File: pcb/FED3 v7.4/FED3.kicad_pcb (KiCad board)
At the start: 4 copper layers, 108 x 50 mm, 89 parts, among them IC1 MC74VHC1GT125, IC2 TB6612FNG, IC4 RTC PCF8523T, J1 Conn_02x03_Odd_Even, Q2 DMP2035U-7, SW1 Sw, SW2 SPST_TACT-KMR2, U1 ATSAMD21G18A, U2 MIC5504-3.3, U3 MCP73831T, X1 ClockXtal, X2 uXtal, X4 microsd, X5 JST-XH-02

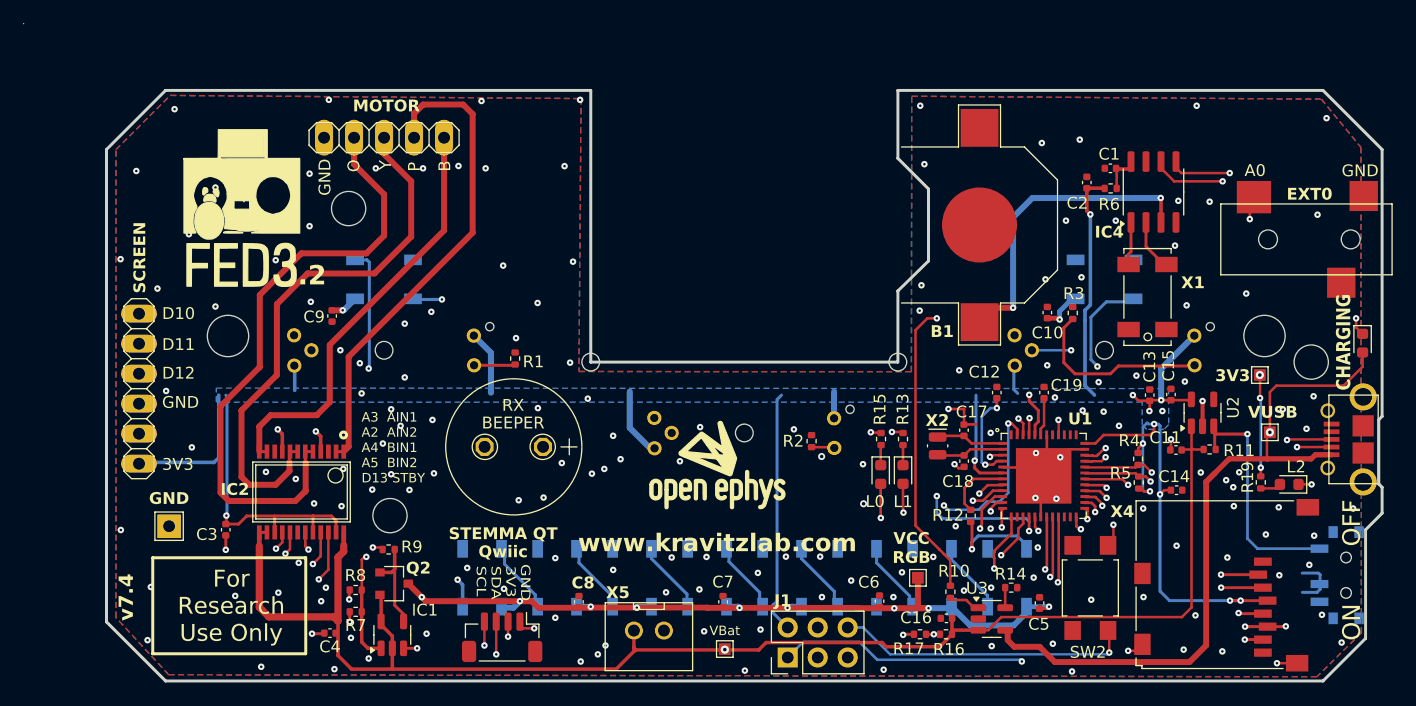
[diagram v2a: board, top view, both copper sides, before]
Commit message: last tunnings
- Top & Bottom Fabrication Layers tuned
- generated Gerbers&Drills files
- generated P&P & BOM files
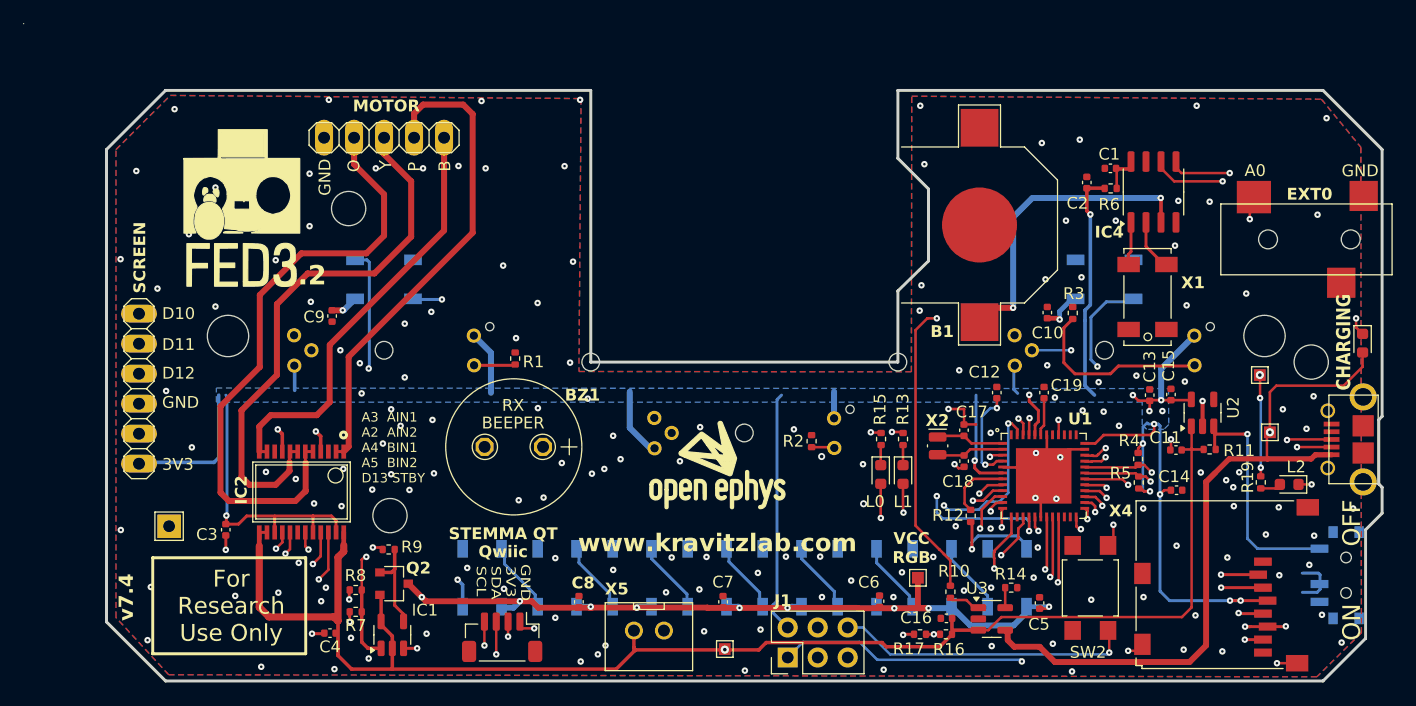
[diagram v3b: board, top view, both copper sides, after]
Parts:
- moved ? 20.0 mm to (192.5, 100.8)
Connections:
- net /controler stage/AREF renamed /Controller Stage/AREF
- net /controler stage/D10 renamed /Controller Stage/D10
- net /controler stage/D11 renamed /Controller Stage/D11
- net /controler stage/D12 renamed /Controller Stage/D12
- net /controler stage/D7 renamed /Controller Stage/D7
- net /controler stage/MISO renamed /Controller Stage/MISO
- net /controler stage/MOSI renamed /Controller Stage/MOSI
- net /controler stage/SCK renamed /Controller Stage/SCK
- net /controler stage/SCL renamed /Controller Stage/SCL
- net /controler stage/SDA renamed /Controller Stage/SDA
- net /controler stage/SD_CS renamed /Controller Stage/SD_CS
- net /controler stage/SQW renamed /Controller Stage/SQW
- net /controler stage/SWCLK renamed /Controller Stage/SWCLK
- net /controler stage/SWDIO renamed /Controller Stage/SWDIO
- net /controler stage/~{RESET} renamed /Controller Stage/~{RESET}

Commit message: 'ultima versão revista; não em tunning com a versão oficial /Kravitz/FED3
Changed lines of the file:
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@@
 		(sheetname "/Controller Stage/")
 		(sheetfile "controler stage.kicad_sch")
+		(attr smd)
 		(fp_circle
 			(center 0 0)
@@
 		(sheetname "/IOs Interface/")
 		(sheetfile "IOs Interface.kicad_sch")
+		(attr smd)
 		(fp_line
 			(start -1.45 0.8)
@@
 			)
 		)
-		(property "MPN" "TB6612FNG,C,8,EL "
+		(property "MPN" "TB6612FNG,C,8,EL"
 			(at 0 0 180)
 			(unlocked yes)
@@
 		(sheetname "/")
 		(sheetfile "FED3.kicad_sch")
+		(attr smd)
 		(fp_line
 			(start 4.128 2.536)
@@
 			)
 		)
-		(property "MPN" "ECS-.327-12.5-17X-C-TR "
+		(property "MPN" "ECS-.327-12.5-17X-C-TR"
 			(at 0 0 270)
 			(unlocked yes)
@@
 		(sheetname "/Controller Stage/")
 		(sheetfile "controler stage.kicad_sch")
+		(attr smd)
 		(fp_line
 			(start -4.1 2)
@@
 			)
 		)
-		(property "Description" "DC DC CONVERTER Boost/Inverter 2output ±40V 1.3A"
+		(property "Description" "BUFFER NON-INVERT 1CH 3-STATE"
 			(at 0 0 90)
 			(unlocked yes)
@@
 		(sheetname "/")
 		(sheetfile "FED3.kicad_sch")
-		(attr through_hole)
+		(attr smd)
 		(fp_line
 			(start -3.75 -2.9)
@@
 		(sheetname "/")
 		(sheetfile "FED3.kicad_sch")
-		(attr through_hole exclude_from_bom)
+		(attr through_hole)
 		(fp_line
 			(start -6.35 -0.635)
@@
 		(sheetname "/IOs Interface/")
 		(sheetfile "IOs Interface.kicad_sch")
-		(attr smd exclude_from_pos_files)
+		(attr smd)
 		(fp_line
 			(start 11 3)
@@
 			)
 		)
-		(property "MPN" "SK6812RGBW-BW"
+		(property "MPN" "XT1511RGBW-BW"
 			(at 0 0 180)
 			(unlocked yes)
@@
 			)
 		)
-		(property "MPN" "SK6812RGBW-BW"
+		(property "MPN" "XT1511RGBW-BW"
 			(at 0 0 270)
 			(unlocked yes)
@@
 			)
 		)
-		(property "MPN" "SSSS811101 "
+		(property "MPN" "SSSS811101"
 			(at 0 0 270)
 			(unlocked yes)
@@
 		(sheetname "/")
 		(sheetfile "FED3.kicad_sch")
+		(attr smd)
 		(fp_line
 			(start -3.4 1.75)
@@
 			)
 		)
-		(property "MPN" "SK6812RGBW-BW"
+		(property "MPN" "XT1511RGBW-BW"
 			(at 0 0 180)
 			(unlocked yes)
@@
 			)
 		)
-		(property "MPN" "SK6812RGBW-BW"
+		(property "MPN" "XT1511RGBW-BW"
 			(at 0 0 270)
 			(unlocked yes)
@@
 			)
 		)
-		(property "MPN" "SK6812RGBW-BW"
+		(property "MPN" "XT1511RGBW-BW"
 			(at 0 0 270)
 			(unlocked yes)
@@
 			)
 		)
-		(property "MPN" "SK6812RGBW-BW"
+		(property "MPN" "XT1511RGBW-BW"
 			(at 0 0 270)
 			(unlocked yes)
@@
 			)
 		)
-		(property "MPN" "SK6812RGBW-BW"
+		(property "MPN" "XT1511RGBW-BW"
 			(at 0 0 270)
 			(unlocked yes)
@@
 			)
 		)
-		(property "MPN" "SK6812RGBW-BW"
+		(property "MPN" "XT1511RGBW-BW"
 			(at 0 0 270)
 			(unlocked yes)
@@
 			)
 		)
-		(property "MPN" "SK6812RGBW-BW"
+		(property "MPN" "XT1511RGBW-BW"
 			(at 0 0 270)
 			(unlocked yes)
@@
 			)
 		)
-		(property "MPN" "SK6812RGBW-BW"
+		(property "MPN" "XT1511RGBW-BW"
 			(at 0 0 270)
 			(unlocked yes)
@@
 		)
 		(layer "F.SilkS")
-	)
-	(gr_arc
-		(start 87.48776 74.351613)
-		(mid 87.487765 74.351635)
-		(end 87.48777 74.351657)
-		(stroke
-			(width 0.01)
-			(type default)
-		)
-		(layer "F.SilkS")
